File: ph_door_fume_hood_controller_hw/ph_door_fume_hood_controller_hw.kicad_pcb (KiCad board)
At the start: 2 copper layers, 160 x 105.2 mm, 247 parts, among them IC1 6N137, IC2 6N137, J1 Conn_01x03, J10 Conn_01x03, J11 Conn_01x02, J12 Conn_01x06, J13 Conn_01x02, J14 Conn_01x03, J15 Conn_01x03, J2 Conn_01x04, J3 CONN_01X04, J4 Conn_01x03, J5 Conn_01x04, J6 Conn_01x02, J7 Conn_01x06, J8 USB_OTG, J9 Conn_01x02, M1 DC-DC-24-12V-200mA, M2 MORSUN_485, Q1 C1815, Q10 A1015, Q11 Q_NMOS_GSD, Q2 Q_PMOS_GDS, Q3 Q_NMOS_GSD, Q4 Q_NMOS_GSD, Q5 C1815, Q6 Q_NMOS_GSD, Q7 Q_NMOS_GSD, Q8 C1815, Q9 Q_NMOS_GSD, U1 74HC123, U10 PC817, U11 MCP4725, U12 ASM1117-3V3, U13 PC817, U14 PC817, U15 LM358, U16 PC817, U17 PC817, U18 PC817, U19 PC817, U2 AD8601, U20 PC817, U21 PC817, U22 PC817, U23 PC817, U3 PC817, U4 PC817, U5 TB6600, U6 PC817, U7 STM32F103C8, U8 ASM1117, U9 XL4015, Y1 Crystal, Y2 32768Mhz

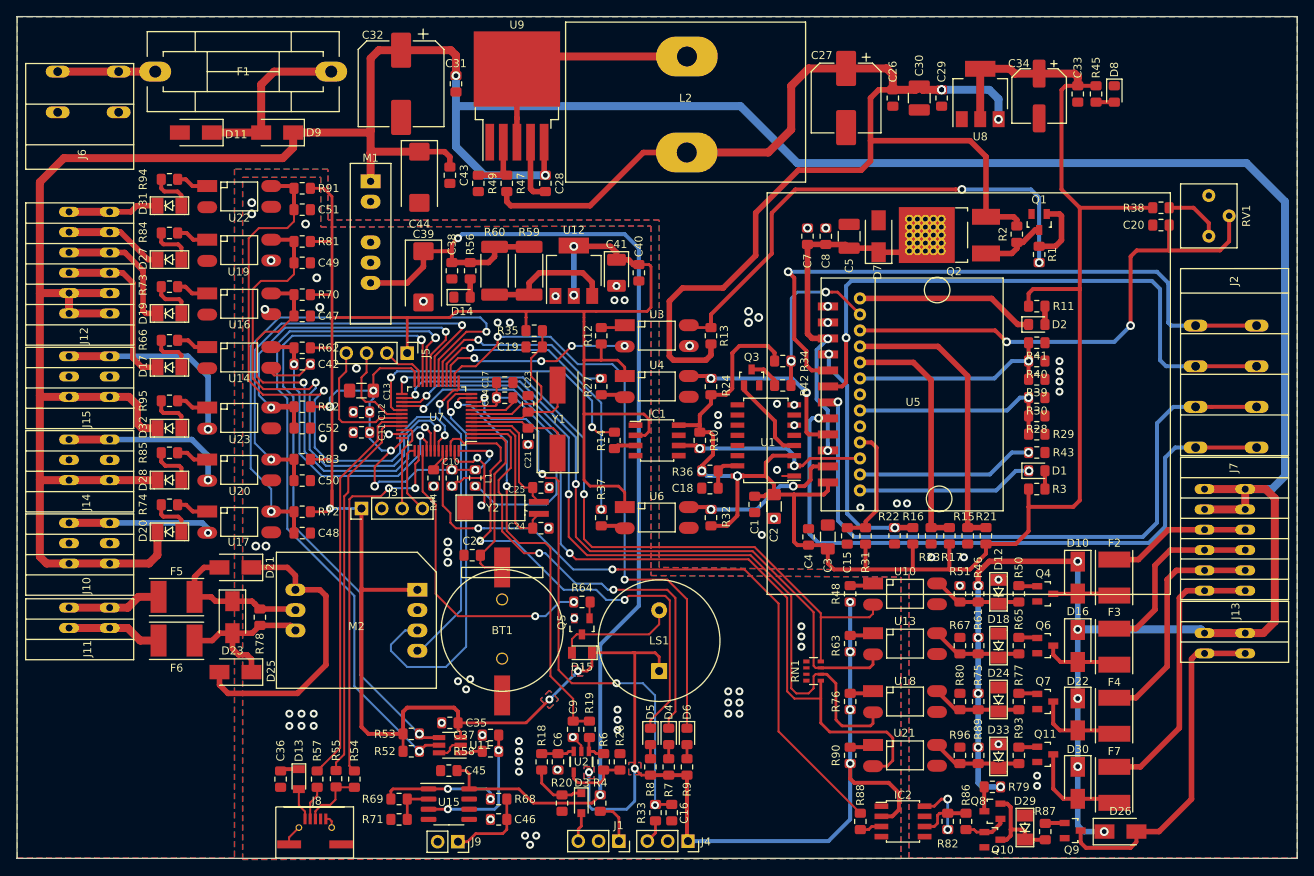
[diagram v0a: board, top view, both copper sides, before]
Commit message: Edit power for fume hood
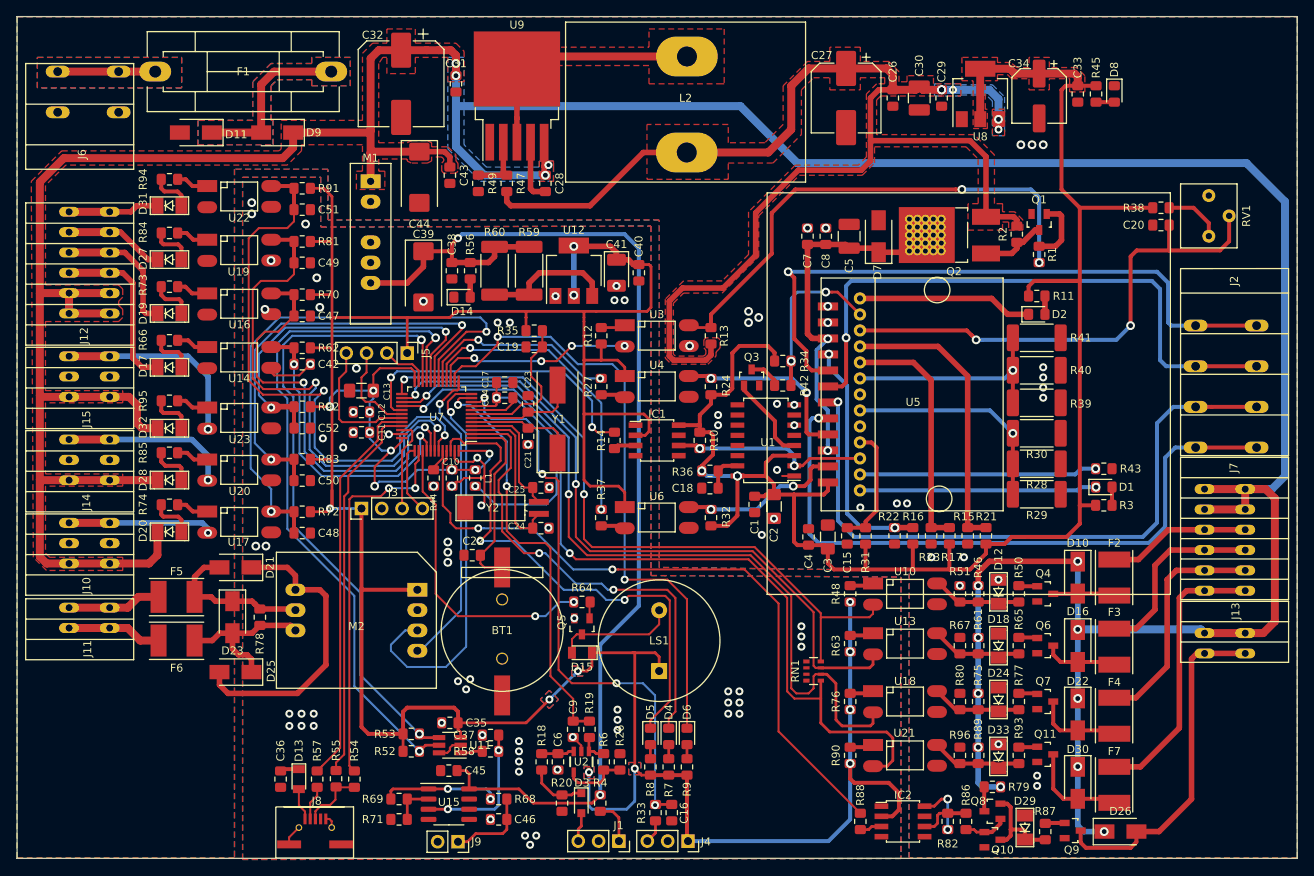
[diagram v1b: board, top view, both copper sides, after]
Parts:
- R28, R29, R30, R39, R40, R41: footprint Resistor_SMD:R_0805_2012Metric_Pad1.15x1.40mm_HandSolder -> Resistor_SMD:R_2512_6332Metric_Pad1.52x3.35mm_HandSolder
- moved D1 8.62 mm to (196.8, 93.6)
- moved R3 8.62 mm to (196.8, 95.9)
- moved R43 8.62 mm to (196.8, 91.3)
- moved R29 7.51 mm to (188.4, 94.5)
- moved R28 5.98 mm to (188.4, 90.7)
- moved R30 4.46 mm to (188.4, 86.9)
- moved R39 2.94 mm to (188.4, 83.1)
- moved D2 1.27 mm to (188.4, 72.0)
- moved R11 1.27 mm to (188.4, 69.7)
- moved R40 1.16 mm to (188.4, 79.0)
- moved R41 0.62 mm to (188.4, 74.9)
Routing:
- net Net-(R43-Pad1): track 22.2 -> 29.8 mm
- net Net-(D1-Pad1): track 22.1 -> 29.7 mm
- net Net-(R28-Pad2): track 26.3 -> 27.9 mm
- net Net-(R39-Pad2): track 26.5 -> 27.7 mm
- net +5V: track 221.3 -> 220.6 mm
- net Net-(D2-Pad1): track 22.4 -> 21.9 mm
- net +24V: vias 12 -> 14
- net GNDPWR: vias 30 -> 33
- net +12V: vias 3 -> 5
- added copper zone on B.Cu, net +12V
- added copper zone on F.Cu, net +12V
- added copper zone on B.Cu, net +24V
- added copper zone on F.Cu, net +24V
- added copper zone on F.Cu, net +5V
- added copper zone on B.Cu, net Net-(D11-Pad1)
- added copper zone on F.Cu, net Net-(D11-Pad1)
- added copper zone on B.Cu, net Net-(F1-Pad1)
- added copper zone on F.Cu, net Net-(F1-Pad1)
- added copper zone on F.Cu, net Net-(L2-Pad2)
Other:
- board text added: "+24VDC"
- board text added: "+24Vdc"
- board text added: "GND"
- board text added: "IN1"
- board text added: "IN2"
- board text added: "IN3"
- board text added: "IN4"

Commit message: The door fume hood
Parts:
- moved R15 2.03 mm to (184.1, 99.7)
- moved R21 2.03 mm to (181.8, 99.7)
- moved R17 1.17 mm to (178.7, 99.7)
- moved R23 1.17 mm to (176.4, 99.7)
- moved R1 0.25 mm to (188.7, 64.3)
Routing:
- net +5V: track 220.6 -> 213.2 mm
- net Net-(C5-Pad1): track 46.6 -> 52.4 mm, vias 2 -> 7
- net +3V3: track 429.2 -> 427.0 mm, vias 20 -> 22
- net /485_RX: track 38.6 -> 40.6 mm
- net Net-(J2-Pad3): track 75.7 -> 74.1 mm, vias 1 -> 3
- net /PWR_STEP: track 63.6 -> 62.1 mm
- net Net-(J2-Pad1): track 83.0 -> 84.2 mm
- net /M1: track 36.2 -> 37.1 mm
- net Net-(J2-Pad4): track 79.8 -> 80.7 mm, vias 1 -> 3
- net /485_TX: track 51.0 -> 50.4 mm
- net /OUTPUT4: track 35.0 -> 35.6 mm
- net Net-(D26-Pad2): track 43.4 -> 42.9 mm
- net Net-(J2-Pad2): track 83.3 -> 83.8 mm, vias 1 -> 2
- net /VREF: vias 2 -> 6
- net Net-(L2-Pad2): vias 0 -> 35
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- added copper zone on B.Cu, net /A
- added copper zone on B.Cu, net /B
- added copper zone on B.Cu, net /INPUT1
- added copper zone on B.Cu, net /INPUT2
- added copper zone on B.Cu, net /INPUT3
- added copper zone on B.Cu, net /INPUT4
- added copper zone on B.Cu, net /OUTPUT1
- added copper zone on F.Cu, net /OUTPUT1
- added copper zone on B.Cu, net /OUTPUT2
- added copper zone on F.Cu, net /OUTPUT2
- added copper zone on B.Cu, net /OUTPUT3
- added copper zone on F.Cu, net /OUTPUT3
- added copper zone on B.Cu, net /OUTPUT4
- added copper zone on F.Cu, net /OUTPUT4
- added copper zone on B.Cu, net /VREF
- added copper zone on F.Cu, net /VREF
- added copper zone on B.Cu, net Net-(D26-Pad2)
- added copper zone on B.Cu, net Net-(J10-Pad3)
- added copper zone on B.Cu, net Net-(J14-Pad3)
- added copper zone on B.Cu, net Net-(J15-Pad3)
- added copper zone on B.Cu, net Net-(J2-Pad1)
- added copper zone on F.Cu, net Net-(J2-Pad1)
- added copper zone on B.Cu, net Net-(J2-Pad2)
- added copper zone on F.Cu, net Net-(J2-Pad2)
- added copper zone on B.Cu, net Net-(J2-Pad3)
- added copper zone on F.Cu, net Net-(J2-Pad3)
- added copper zone on B.Cu, net Net-(J2-Pad4)
- added copper zone on F.Cu, net Net-(J2-Pad4)
- added copper zone on B.Cu, net Net-(L2-Pad2)
- added copper zone on F.Cu, net Net-(R28-Pad2)
- added copper zone on F.Cu, net Net-(R39-Pad2)
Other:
- outline, holes or cut-outs redrawn
- board text added: "+12Vdc"
- board text added: "+3V3"
- board text added: "A"
- board text added: "Analog1"
- board text added: "Analog2"
- board text added: "B"
- board text added: "DAC"
- board text added: "INPUT1"
- board text added: "INPUT2"
- board text added: "INPUT3"
- board text added: "INPUT4"
- board text added: "Sensor1"
- board text added: "Sensor2"
- board text added: "Sensor3"
- board text added: "USB"
- board text removed: "IN1"
- board text removed: "IN2"
- board text removed: "IN3"
- board text removed: "IN4"

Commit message: Edited position board analyzer
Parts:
- added G***: LOGO, PH_Footprint:logo, F.Cu at (210.8, 47.0)
- added G***: LOGO, PH_Footprint:logo, B.Cu at (210.8, 47.0)
- added REF**: Vit-4mm, VinhTho_Lib:Vit-4mm, F.Cu at (64.0, 37.8)
- added REF**: Vit-4mm, VinhTho_Lib:Vit-4mm, F.Cu at (64.0, 136.9)
- added REF**: Vit-4mm, VinhTho_Lib:Vit-4mm, F.Cu at (217.9, 136.9)
- added REF**: Vit-4mm, VinhTho_Lib:Vit-4mm, F.Cu at (217.9, 37.8)
- moved R28 0.51 mm to (188.9, 90.7)
- moved R29 0.51 mm to (188.9, 94.5)
- moved R30 0.51 mm to (188.9, 86.9)
- moved R39 0.51 mm to (188.9, 83.1)
- moved R40 0.51 mm to (188.9, 79.0)
- moved R41 0.51 mm to (188.9, 74.9)
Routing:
- net Net-(R28-Pad2): track 27.9 -> 28.4 mm, vias 1 -> 5
- net Net-(R39-Pad2): track 27.7 -> 28.2 mm, vias 1 -> 4
- added copper zone on B.Cu, net Net-(R28-Pad2)
- added copper zone on B.Cu, net Net-(R39-Pad2)

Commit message: Update
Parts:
- IC2: footprint VinhTho_Lib:Diodes_PSOP-8 -> ph_kicad_lib:SMDIP-8_W9.53mm
- moved R82 3.81 mm to (179.6, 132.3), turned to 270 degrees
- moved R88 2.68 mm to (163.7, 135.6)
- moved R86 1.91 mm to (179.6, 137.3), turned to 270 degrees
- moved IC2 1.78 mm to (171.7, 133.6)
- moved R90 1.27 mm to (165.1, 125.9)
- moved U21 1.27 mm to (172.0, 125.9)
- moved R29 1.02 mm to (188.9, 95.5)
- moved R76 1.02 mm to (165.1, 119.4)
- moved U18 1.02 mm to (172.0, 119.4)
- moved D2 0.76 mm to (188.4, 71.2)
- moved R11 0.76 mm to (188.4, 68.9)
- moved R28 0.63 mm to (188.9, 91.3)
- moved R30 0.38 mm to (188.9, 87.2)
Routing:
- net Net-(J2-Pad3): track 74.1 -> 81.6 mm
- net Net-(J2-Pad4): track 80.7 -> 87.6 mm
- net +3V3: track 427.0 -> 420.5 mm
- net /M3: track 31.0 -> 35.7 mm
- net Net-(IC2-Pad6): track 6.44 -> 11.0 mm, vias 0 -> 3
- net Net-(IC2-Pad8): track 7.07 -> 4.58 mm, vias 2 -> 0
- net Net-(D33-Pad1): track 11.7 -> 14.1 mm, vias 0 -> 2
- net Net-(D24-Pad1): track 11.4 -> 13.4 mm, vias 0 -> 2
- net /O3: track 98.5 -> 97.0 mm
- net /PWM: track 85.2 -> 86.7 mm
- net Net-(IC2-Pad3): track 2.80 -> 3.98 mm
- net Net-(D1-Pad1): track 29.7 -> 30.8 mm
- net /O4: track 104.9 -> 103.8 mm
- net Net-(D2-Pad1): track 21.9 -> 22.8 mm
- net /VREF: track 63.1 -> 64.0 mm
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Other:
- board text added: "+24V"
- board text added: "OUT1"
- board text added: "OUT1A"
- board text added: "OUT1B"
- board text added: "OUT2"
- board text added: "OUT2A"
- board text added: "OUT2B"
- board text added: "OUT3"
- board text added: "OUT4"
- board text added: "PWM"
- board text added: "The fume hood controller"
